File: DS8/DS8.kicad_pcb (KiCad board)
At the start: 2 copper layers, 65.5 x 110 mm, 92 parts, among them P1 CONN-02x05, Q1 3904, Q2 3904, U0 LM13700, U1 LM385, U2 LM385, U3 LM385, U4 LM385, U5 LM385, U6 KA78L05

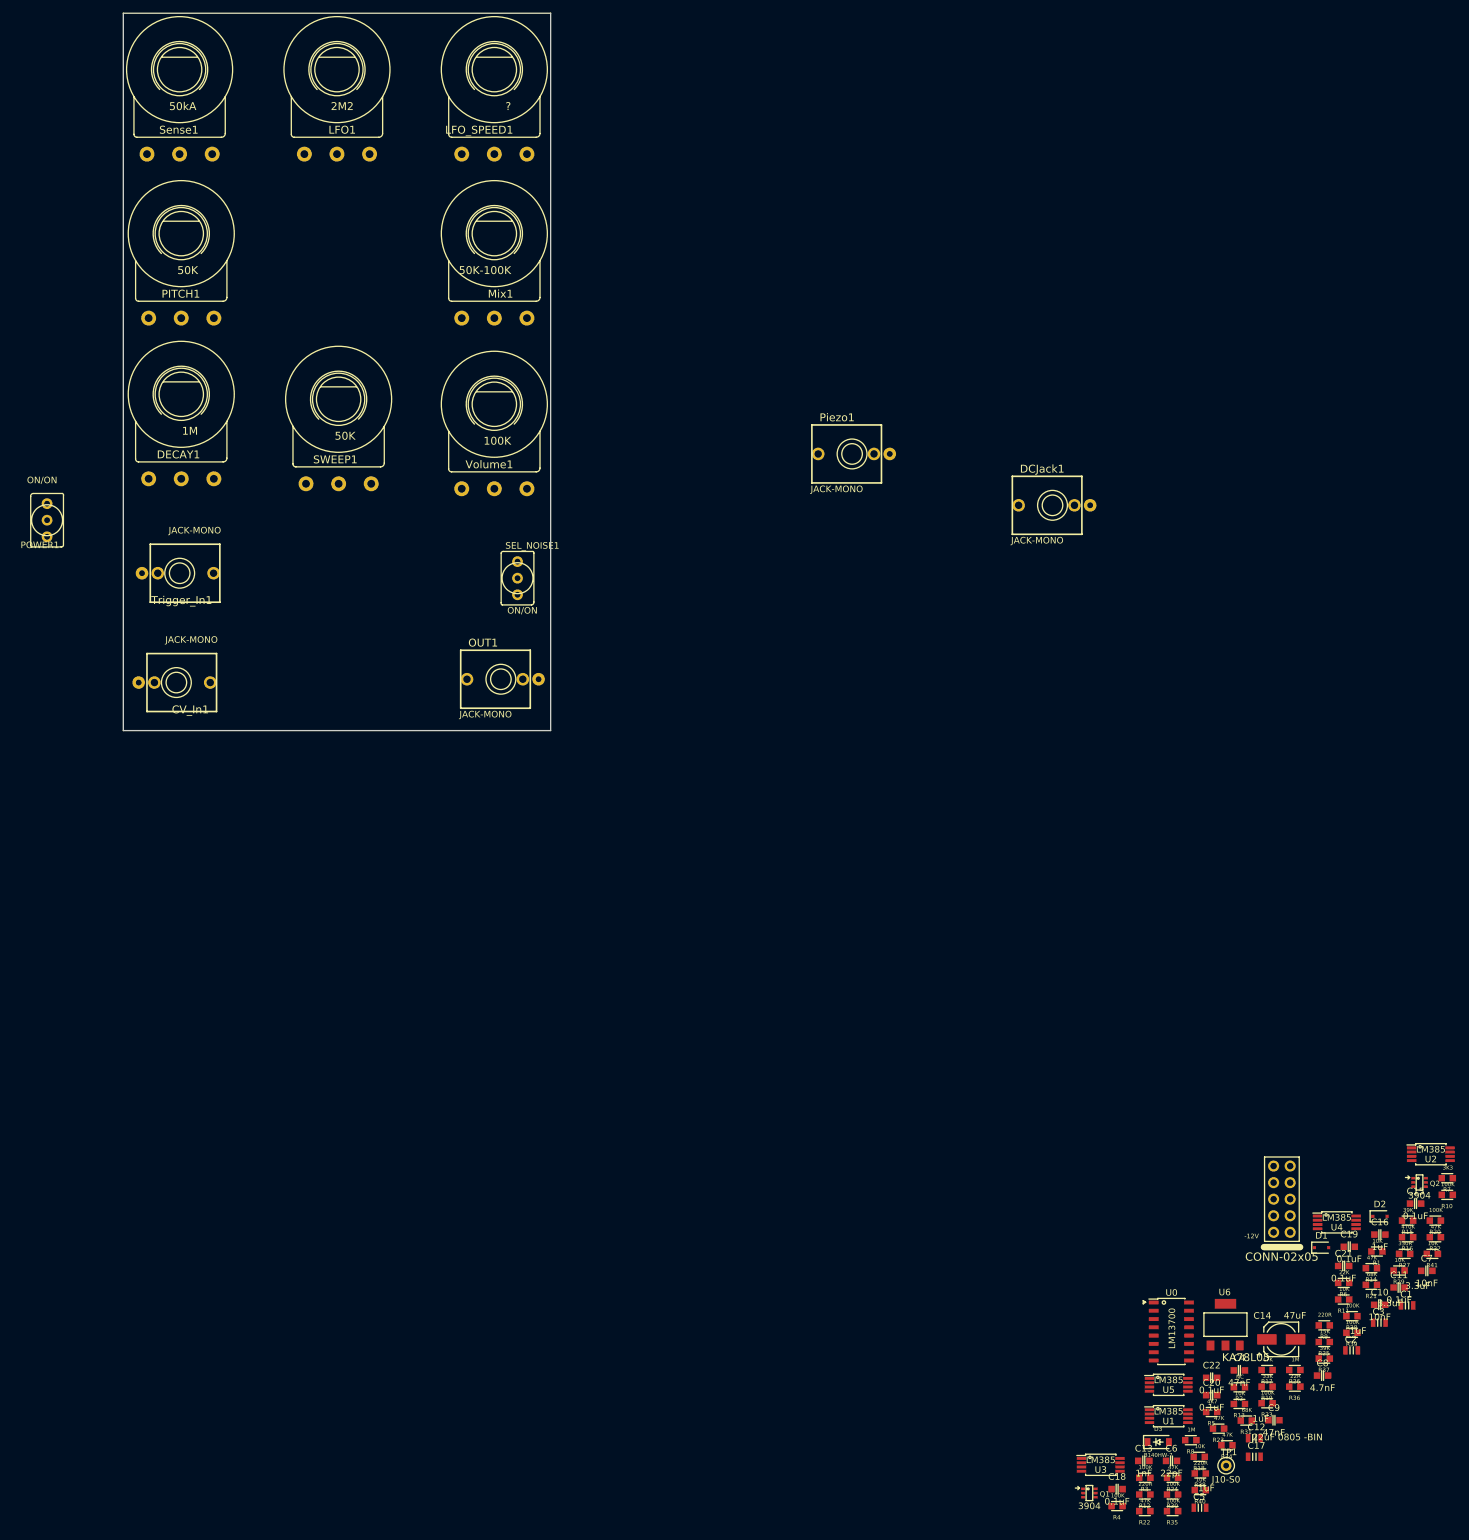
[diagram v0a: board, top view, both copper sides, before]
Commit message: settled on hardware placement
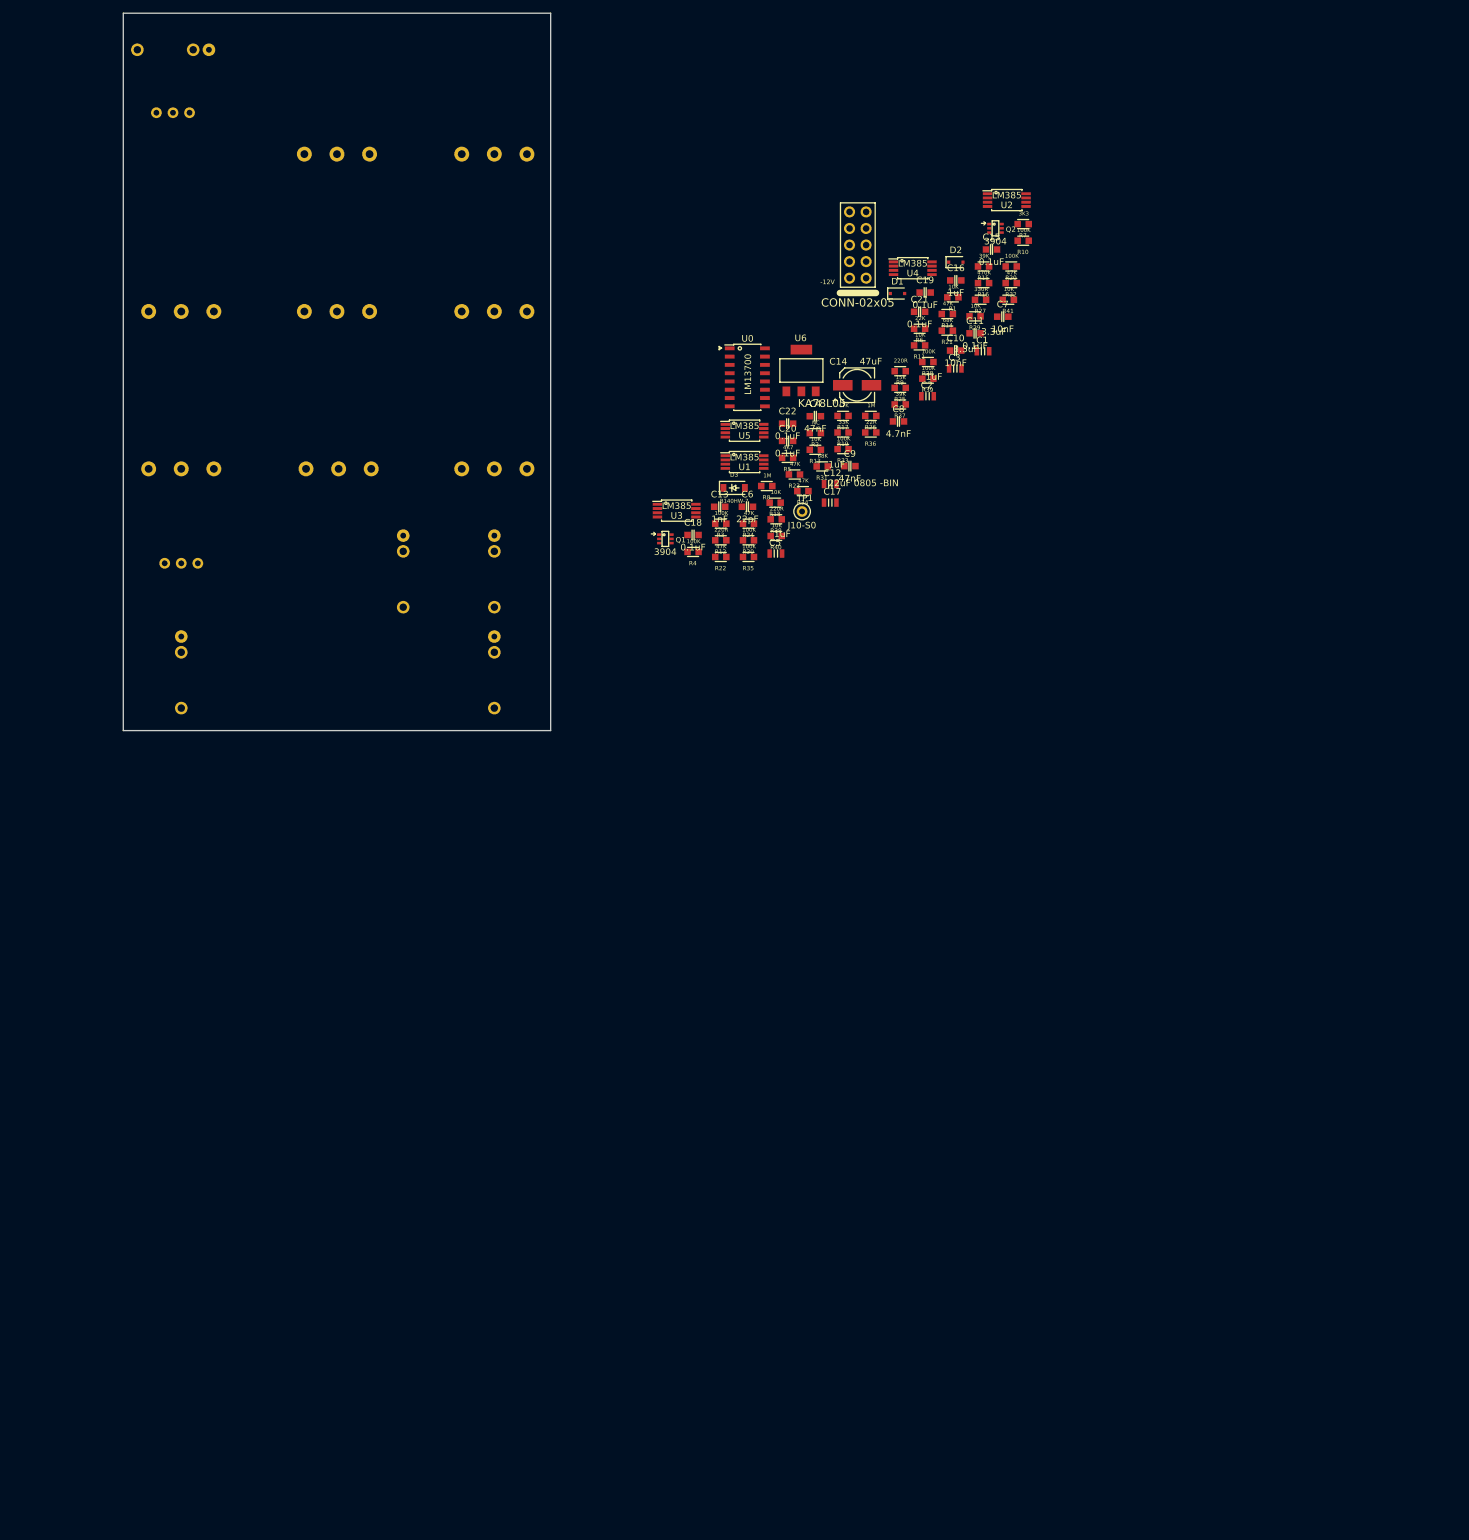
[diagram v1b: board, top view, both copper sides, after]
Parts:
- CV_In1, DCJack1, DECAY1, LFO1, LFO_SPEED1, Mix1, OUT1, PITCH1, POWER1, Piezo1, SEL_NOISE1, SWEEP1, Sense1, Trigger_In1, Volume1: moved to B.Cu
- moved C1 160.1 mm to (131.8, -58.2)
- moved C10 160.1 mm to (127.6, -58.3)
- moved C11 160.1 mm to (130.6, -60.9)
- moved C12 160.1 mm to (108.4, -37.8)
- moved C13 160.1 mm to (91.5, -34.3)
- moved C14 160.1 mm to (112.5, -53.0)
- moved C15 160.1 mm to (133.1, -73.8)
- moved C16 160.1 mm to (127.7, -69.0)
- moved C17 160.1 mm to (108.4, -35.0)
- moved C18 160.1 mm to (87.4, -30.0)
- moved C19 160.1 mm to (123.0, -67.2)
- moved C2 160.1 mm to (123.3, -51.3)
- moved C20 160.1 mm to (101.9, -44.4)
- moved C22 160.1 mm to (101.9, -47.1)
- moved C3 160.1 mm to (127.6, -55.5)
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
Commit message: continued work on pcb
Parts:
- moved R20 165.4 mm to (-16.8, -8.13)
- moved R32 160.8 mm to (-24.6, -66.0)
- moved R27 157.8 mm to (-11.9, -0.25)
- moved TP1 157.3 mm to (-48.8, -70.4)
- moved R16 155.1 mm to (-18.0, -29.0)
- moved Q2 154.8 mm to (-8.38, -15.7)
- moved U2 152.2 mm to (-16.3, -69.1)
- moved C21 149.7 mm to (-27.2, -74.7)
- moved C7 148.3 mm to (-8.38, -25.1)
- moved C10 148.0 mm to (-11.9, -8.89)
- moved R33 147.9 mm to (-35.8, -65.5)
- moved R28 146.8 mm to (-22.9, -69.3)
- moved C15 146.7 mm to (-11.7, -50.5)
- moved R41 145.1 mm to (-6.35, -95.5)
- moved R34 143.2 mm to (-35.3, -69.1)
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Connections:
- Q1 pad 3: Net-(C10-Pad2) -> Net-(Q1-Pad3)
- Q1 pad 4: GND -> Net-(Q1-Pad4)
- Q1 pad 5: Net-(C13-Pad1) -> Net-(Q1-Pad5)
- Q2 pad 3: Net-(Q2-Pad3) -> Net-(C10-Pad2)
- Q2 pad 4: Net-(Q2-Pad4) -> GND
- Q2 pad 5: Net-(Q2-Pad5) -> Net-(C13-Pad1)

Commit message: forgot to save
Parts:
- added -12V1: -12V, 4ms_TestPoint:TestPoint_WireHole, F.Cu at (-26.7, -114.3)
- added ENV1: TP, 4ms_TestPoint:TestPoint_Pad_10, F.Cu at (-26.2, -122.8)
- added ENV2: TP, 4ms_TestPoint:TestPoint_Pad_10, F.Cu at (-26.2, -118.4)
- added LFO1: TP, 4ms_TestPoint:TestPoint_Pad_10, F.Cu at (-21.6, -122.8)
- added LFO2: TP, 4ms_TestPoint:TestPoint_Pad_10, F.Cu at (-21.6, -118.4)
- added NSE1: TP, 4ms_TestPoint:TestPoint_Pad_10, F.Cu at (-17.1, -122.8)
- added NSE2: TP, 4ms_TestPoint:TestPoint_Pad_10, F.Cu at (-17.1, -118.4)
- added VCO1: TP, 4ms_TestPoint:TestPoint_Pad_10, F.Cu at (-12.5, -122.8)
- added VCO2: TP, 4ms_TestPoint:TestPoint_Pad_10, F.Cu at (-12.5, -118.4)
- renumbered LFO1 to LFO_LVL1
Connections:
- LFO_LVL1 pad 2: /LFO_LEVEL -> Net-(LFO1-Pad1)
- R18 pad 2: /MIX_POT_3 -> Net-(NSE1-Pad1)
- R29 pad 2: /MIX_POT_1 -> Net-(R29-Pad2)
- U1 pad 6: Net-(D2-Pad2) -> Net-(ENV1-Pad1)
- U1 pad 7: Net-(D2-Pad2) -> Net-(ENV1-Pad1)

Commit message: Finished first draft of layout
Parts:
- removed Piezo1: JACK-MONO, 4ms_Jack:EighthInch_PJ398SM
- removed TP1: J10-S0, 4ms_TestPoint:TestPoint_WireHole
- added PIEZO1: TP, 4ms_TestPoint:TestPoint_WireHole, F.Cu at (43.4, -27.5)
- added PIEZO2: TP, 4ms_TestPoint:TestPoint_WireHole, F.Cu at (48.9, -29.8)
- moved ENV1 86.2 mm to (58.3, -105.9)
- moved ENV2 81.9 mm to (54.7, -105.9)
- moved R34 72.0 mm to (32.4, -44.8)
- moved C21 71.3 mm to (39.2, -48.6)
- moved LFO2 67.6 mm to (36.3, -83.5)
- moved LFO1 67.1 mm to (32.7, -83.5)
- moved R33 66.5 mm to (28.4, -48.1), turned to 270 degrees
- moved R28 64.5 mm to (36.4, -43.9), turned to 270 degrees
- moved C18 63.6 mm to (39.5, -57.1), turned to 270 degrees
- moved R32 63.5 mm to (34.9, -43.9), turned to 270 degrees
- moved R41 60.9 mm to (38.8, -54.7), turned to 180 degrees
- moved Q1 60.8 mm to (36.7, -51.6), turned to 270 degrees
- moved VCO1 60.3 mm to (17.4, -70.5), turned to 180 degrees
- moved R24 57.8 mm to (40.1, -46.0), turned to 270 degrees
- moved R40 56.4 mm to (38.0, -57.1), turned to 90 degrees
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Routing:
- net +5V: track 0.00 -> 201.3 mm, vias 0 -> 8
- net /VCO: track 0.00 -> 133.5 mm, vias 0 -> 6
- net GND: track 0.00 -> 91.1 mm, vias 0 -> 14
- net Net-(Sense1-Pad3): track 0.00 -> 75.8 mm
- net /VCA_P5: track 0.00 -> 75.1 mm, vias 0 -> 2
- net Net-(C3-Pad2): track 0.00 -> 66.1 mm
- net /VREF: track 0.00 -> 65.8 mm, vias 0 -> 5
- net Net-(C1-Pad2): track 0.00 -> 34.8 mm
- net Net-(R29-Pad2): track 0.00 -> 27.6 mm, vias 0 -> 2
- net Net-(C2-Pad1): track 0.00 -> 27.2 mm
- net Net-(R28-Pad2): track 0.00 -> 21.7 mm, vias 0 -> 2
- net Net-(C4-Pad1): track 0.00 -> 20.7 mm, vias 0 -> 1
- net /MIX_POT_3: track 0.00 -> 17.0 mm
- net Net-(LFO_SPEED1-Pad1): track 0.00 -> 15.2 mm
- net Net-(R3-Pad2): track 0.00 -> 14.9 mm
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- added copper zone on B.Cu, net GND
- added copper zone on F.Cu, net GND

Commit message: cleaned up references
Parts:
- moved C18 0.06 mm to (39.6, -57.0)
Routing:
- net Net-(NSE1-Pad1): track 0.00 -> 54.3 mm, vias 0 -> 2
- net GND: vias 14 -> 21
- net /VCO: vias 6 -> 7

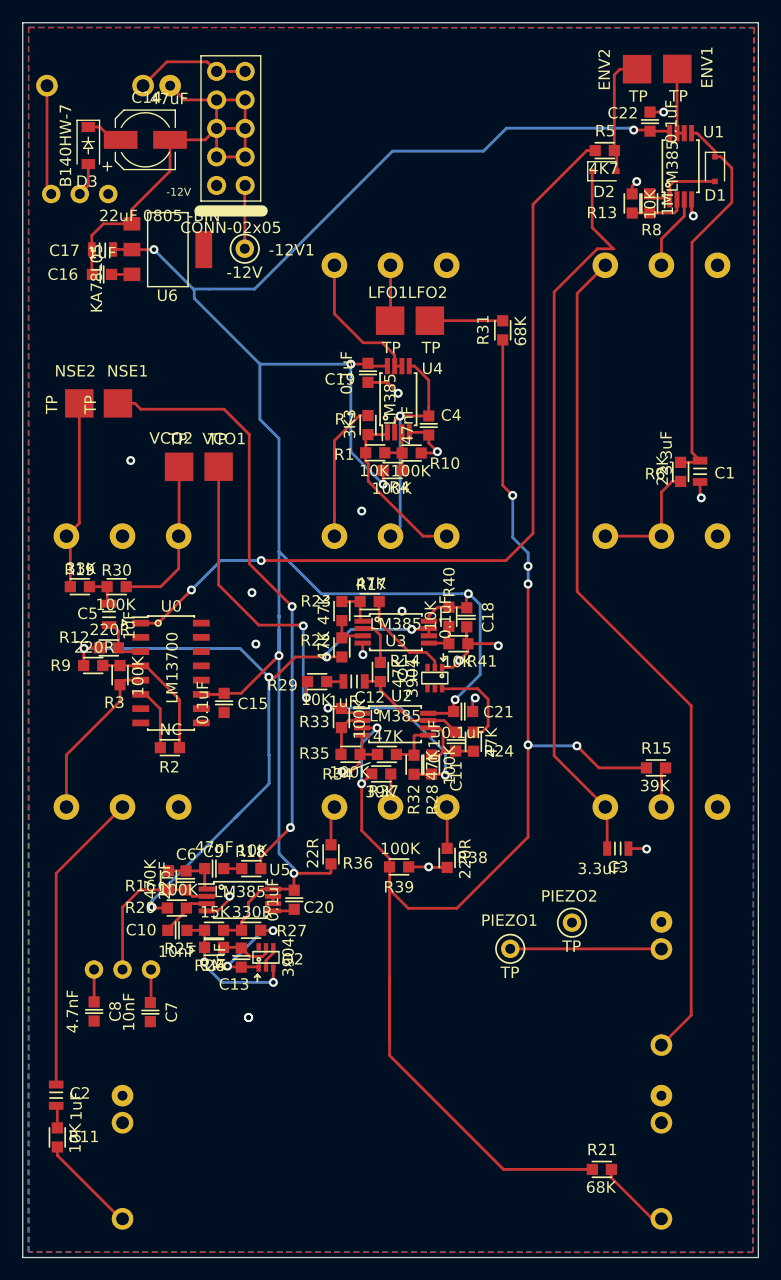
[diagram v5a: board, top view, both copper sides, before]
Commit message: redid GND - used tracks instead of GND plane - generated GERBERS
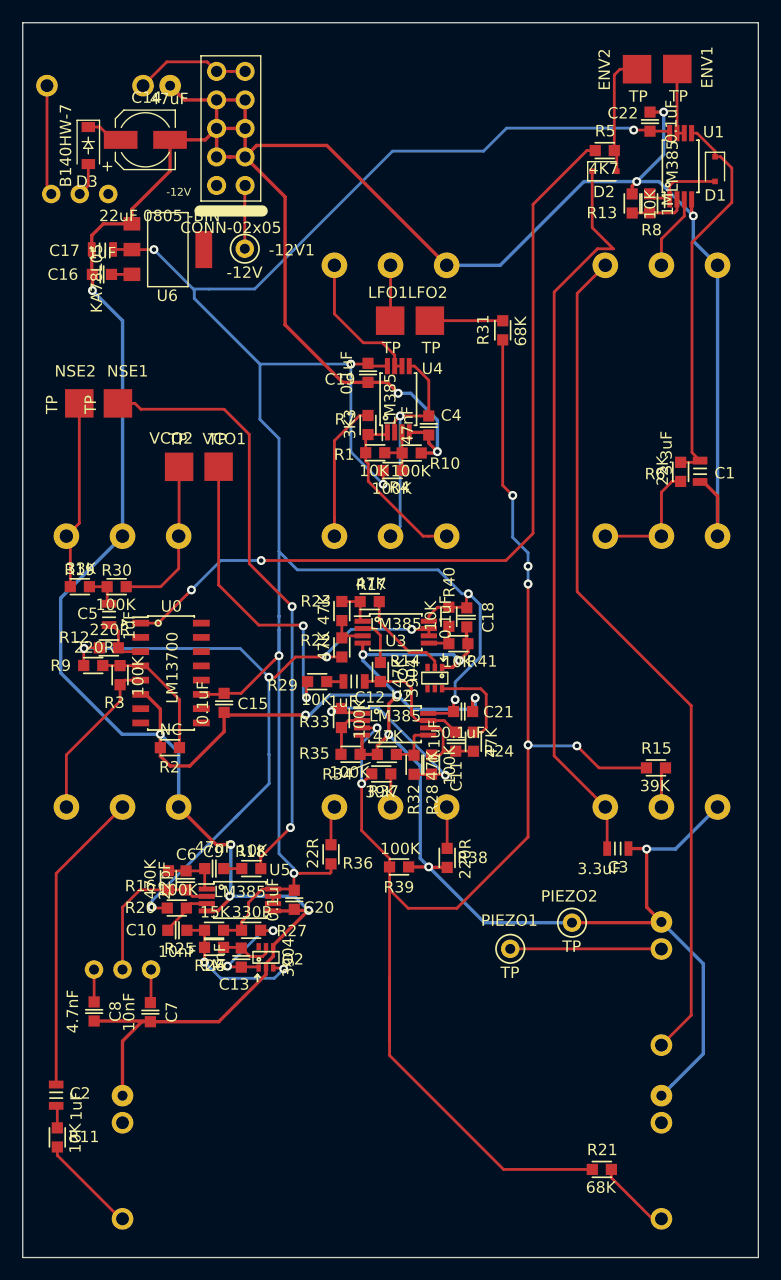
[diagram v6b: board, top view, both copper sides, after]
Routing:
- net GND: track 91.1 -> 439.5 mm, vias 21 -> 18
- net Net-(R28-Pad2): track 21.7 -> 20.2 mm
- net Net-(C11-Pad1): track 10.4 -> 11.3 mm
- net Net-(C10-Pad2): track 12.7 -> 13.4 mm
- removed copper zone on B.Cu, net GND
- removed copper zone on F.Cu, net GND

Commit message: generated gerbers and ordered from oshpark
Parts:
- R12, R38, R9: value 220R -> 220R. ??
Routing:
- net Net-(C3-Pad2): track 66.1 -> 63.7 mm
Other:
- board text added: "DS8 DEV BOARD"
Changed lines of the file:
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@@
   (general
     (thickness 1.6)
-    (drawings 5)
-    (tracks 649)
+    (drawings 6)
+    (tracks 647)
     (zones 0)
     (modules 101)
@@
     (solder_mask_min_width 0.25)
     (aux_axis_origin 0 0)
-    (visible_elements 7FFDEFFF)
+    (visible_elements 7FF4EFFF)
     (pcbplotparams
       (layerselection 0x010fc_ffffffff)
@@
       (psa4output false)
       (plotreference true)
-      (plotvalue true)
+      (plotvalue false)
       (plotinvisibletext false)
       (padsonsilk false)
@@
       (effects (font (size 1.016 1.016) (thickness 0.15)))
     )
-    (fp_text value 220R (at 0.09 -1.61 90) (layer F.SilkS)
+    (fp_text value "220R. ??" (at 0.09 -1.61 90) (layer F.SilkS)
       (effects (font (size 1.016 1.016) (thickness 0.15)))
     )
@@
       (effects (font (size 1.016 1.016) (thickness 0.15)))
     )
-    (fp_text value 220R (at 0.09 -1.61) (layer F.SilkS)
+    (fp_text value "220R. ??" (at 0.09 -1.61) (layer F.SilkS)
       (effects (font (size 1.016 1.016) (thickness 0.15)))
     )
@@
       (effects (font (size 1.016 1.016) (thickness 0.15)))
     )
-    (fp_text value 220R (at 0.09 -1.61) (layer F.SilkS)
+    (fp_text value "220R. ??" (at 0.09 -1.61) (layer F.SilkS)
       (effects (font (size 1.016 1.016) (thickness 0.15)))
     )
@@
     )
   )
+  (gr_text "DS8 DEV BOARD" (at 32.96 -3.08) (layer F.SilkS)
+    (effects (font (size 3 3) (thickness 0.75)))
+  )
   (gr_line (start 29.4 -43.47) (end 30.95 -44.09) (layer F.SilkS) (width 0.12))
   (gr_line (start 0 -110) (end 65.532 -110) (layer Edge.Cuts) (width 0.05))
@@
   (segment (start 52.06 -39.968) (end 51.896 -40.132) (width 0.25) (layer F.Cu) (net 5))
   (segment (start 52.06 -36.43) (end 52.06 -39.968) (width 0.25) (layer F.Cu) (net 5))
-  (segment (start 50.73 -91.75) (end 52.619999 -89.860001) (width 0.25) (layer F.Cu) (net 5))
   (segment (start 50.753001 -41.274999) (end 51.896 -40.132) (width 0.25) (layer F.Cu) (net 5))
-  (segment (start 50.73 -96.77) (end 50.73 -91.75) (width 0.25) (layer F.Cu) (net 5))
-  (segment (start 52.619999 -89.860001) (end 51.191359 -89.860001) (width 0.25) (layer F.Cu) (net 5))
-  (segment (start 51.191359 -89.860001) (end 47.34 -86.008642) (width 0.25) (layer F.Cu) (net 5))
-  (segment (start 47.34 -86.008642) (end 47.34 -44.688) (width 0.25) (layer F.Cu) (net 5))
   (segment (start 47.34 -44.688) (end 50.753001 -41.274999) (width 0.25) (layer F.Cu) (net 5))
+  (segment (start 47.34 -90.29) (end 47.34 -44.688) (width 0.25) (layer F.Cu) (net 5))
+  (segment (start 50.73 -93.68) (end 47.34 -90.29) (width 0.25) (layer F.Cu) (net 5))
+  (segment (start 50.73 -96.77) (end 50.73 -93.68) (width 0.25) (layer F.Cu) (net 5))
   (segment (start 36.17 -75.72) (end 36.17 -74.97) (width 0.25) (layer F.Cu) (net 6))
   (segment (start 36.17 -78.15) (end 36.17 -75.72) (width 0.25) (layer F.Cu) (net 6))
